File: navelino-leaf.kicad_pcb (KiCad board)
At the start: 2 copper layers, 54 x 62.5 mm, 13 parts, among them IC1 ATTINY45-S, P2 CONN_01X04, P3 CONN_02X03

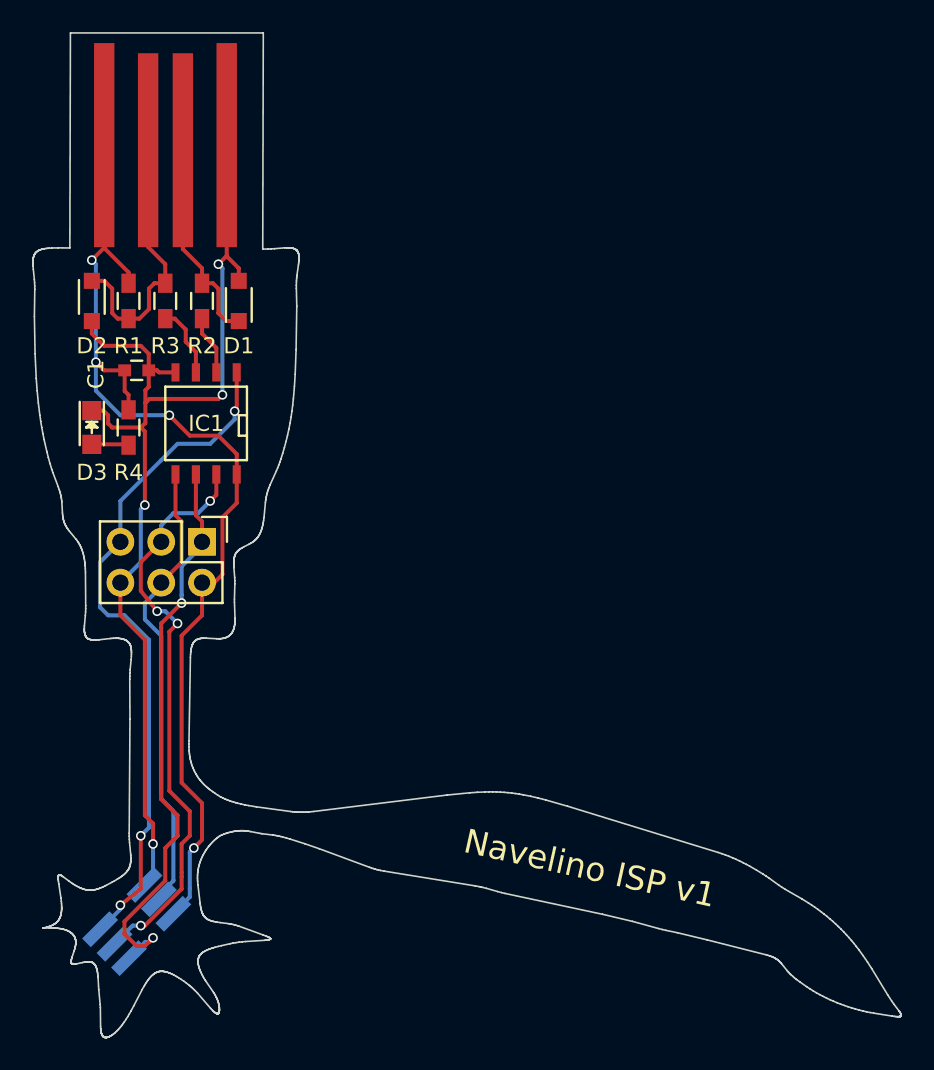
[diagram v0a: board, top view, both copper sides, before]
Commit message: Corregido footprint del SOIC8 Re-enrutado de ISP SMD Un poco de amor al Silkscreen de los diodos
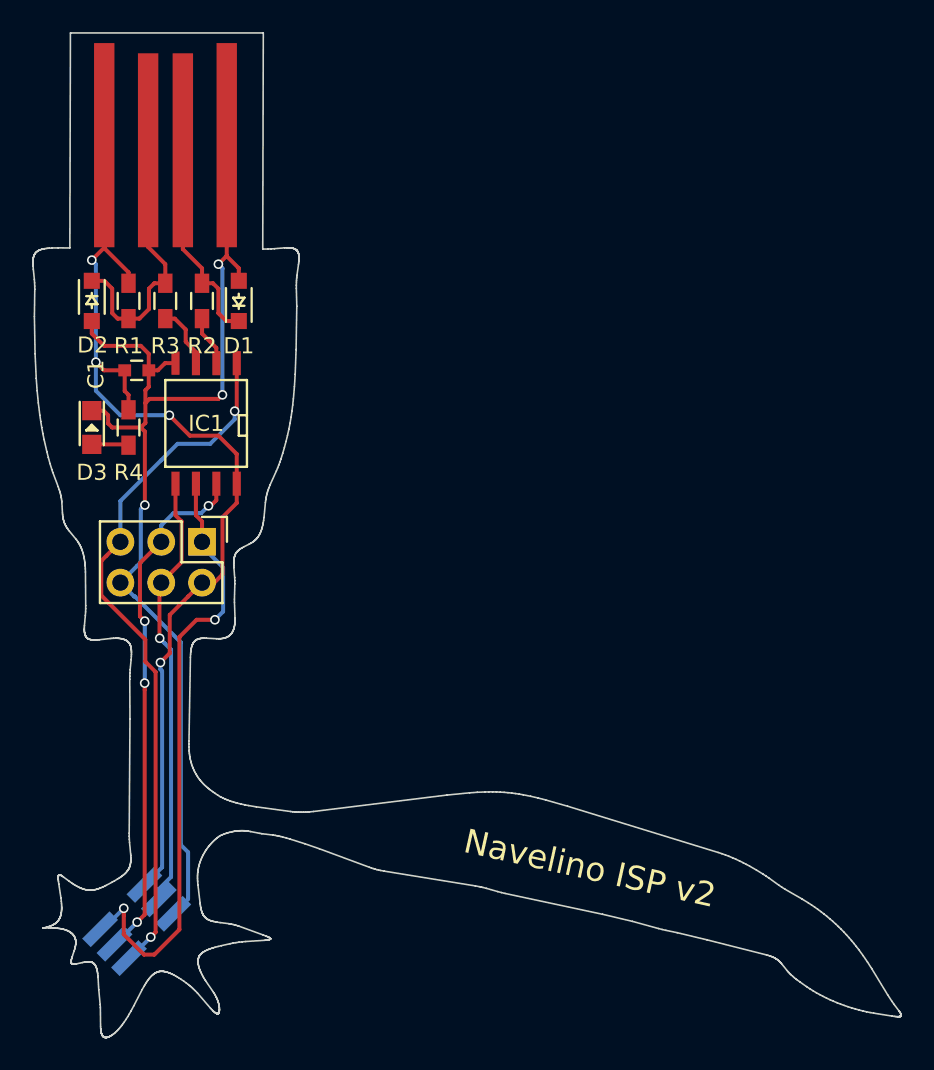
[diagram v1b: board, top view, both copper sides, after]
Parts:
- D1: footprint Diodes_SMD:SOD-323_HandSoldering -> SOD-323_HandSoldering
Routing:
- net MISO: track 36.3 -> 39.6 mm
- net GND: track 68.1 -> 71.1 mm, vias 4 -> 3
- net SCK: track 36.3 -> 33.9 mm
- net VCC: track 71.6 -> 70.3 mm
- net RESET: track 42.6 -> 43.2 mm, vias 3 -> 2
- net MOSI: track 29.4 -> 29.0 mm, vias 0 -> 1
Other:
- board text added: "Navelino ISP v2"
- board text removed: "Navelino ISP v1"
